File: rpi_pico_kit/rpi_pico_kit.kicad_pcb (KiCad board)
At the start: 2 copper layers, 99.1 x 99.1 mm, 200 parts, among them J1 DC Jack 5.5x2.1mm, J10 OLED Display SSD1306, J11 Conn_01x04_Male, J12 Conn_01x04_Male, J13 AudioJack-CUI-SJ-3523-SMT, J14 AudioJack-CUI-SJ-3523-SMT, J2 USB_B, J3 Conn_01x03_Male, J4 DB15_Female, J5 HDMI_A, J6 Conn_01x08_Male, J7 Conn_01x08_Male, J8 Conn_01x08_Male, J9 Micro_SD_Card_Det, Q1 DMN63D8L-7, Q2 DMN63D8L-7, Q3 DMN63D8L-7, Q4 DMN63D8L-7, Q5 DMN63D8L-7, Q6 DMN63D8L-7, Q7 DMN63D8L-7, SW1 SW_Push, SW10 SW_Push, SW2 RotaryEncoder_Switch, SW3 SW_Push, SW4 SW_Push, SW5 SW_Push, SW6 SW_Push, SW7 SW_Push, SW8 SW_Push, SW9 SW_Push, U1 RPi Pico, U10 74LVC2G34GV, U11 PCM5101A, U2 NCP1117-3.3_SOT223, U3 RP2040, U4 W25Q16JVSSIQ, U5 74HC14, U6 74HC14, U7 MCP23S08-xSO, U8 AT24CS32, U9 NCP115-3.3_SOT23-5, Y1 12MHz

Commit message: pcb changes
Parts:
- removed JP2, JP3, JP4, JP5, JP6: SolderJumper_2_Bridged, Jumper:SolderJumper-2_P1.3mm_Bridged_RoundedPad1.0x1.5mm
- TP3: footprint TestPoint:TestPoint_Pad_D1.5mm -> TestPoint:TestPoint_Pad_D1.0mm
- moved LED2 140.2 mm to (149.4, -14.7)
- moved LED3 128.2 mm to (149.2, -10.7)
- moved LED4 128.2 mm to (149.2, -6.86)
- moved R1 121.4 mm to (24.3, 34.0)
- moved D3 80.4 mm to (126.0, -19.6)
- moved R17 77.0 mm to (126.0, -12.7)
- moved R18 67.1 mm to (126.0, -9.65)
- moved R6 60.3 mm to (82.0, 50.8)
- moved RN3 59.2 mm to (97.3, 57.4)
- moved C18 57.4 mm to (126.0, -6.60)
- moved JP1 54.1 mm to (27.9, -6.86)
- moved R14 51.8 mm to (27.9, -10.4)
- moved R16 50.8 mm to (126.0, -15.7)
- moved C3 47.5 mm to (76.7, -13.0)
- moved Y1 47.1 mm to (90.2, 24.4)
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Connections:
- R13 pad 2: Net-(JP6-A) -> /~{RESET}
- RN14 pad 5: Net-(JP3-A) -> /SWDIO
- RN14 pad 6: Net-(JP2-A) -> /SWCLK
- U3 pad 6: Net-(JP4-A) -> /DEBUGGER_RX
- U3 pad 7: Net-(JP5-A) -> /DEBUGGER_TX

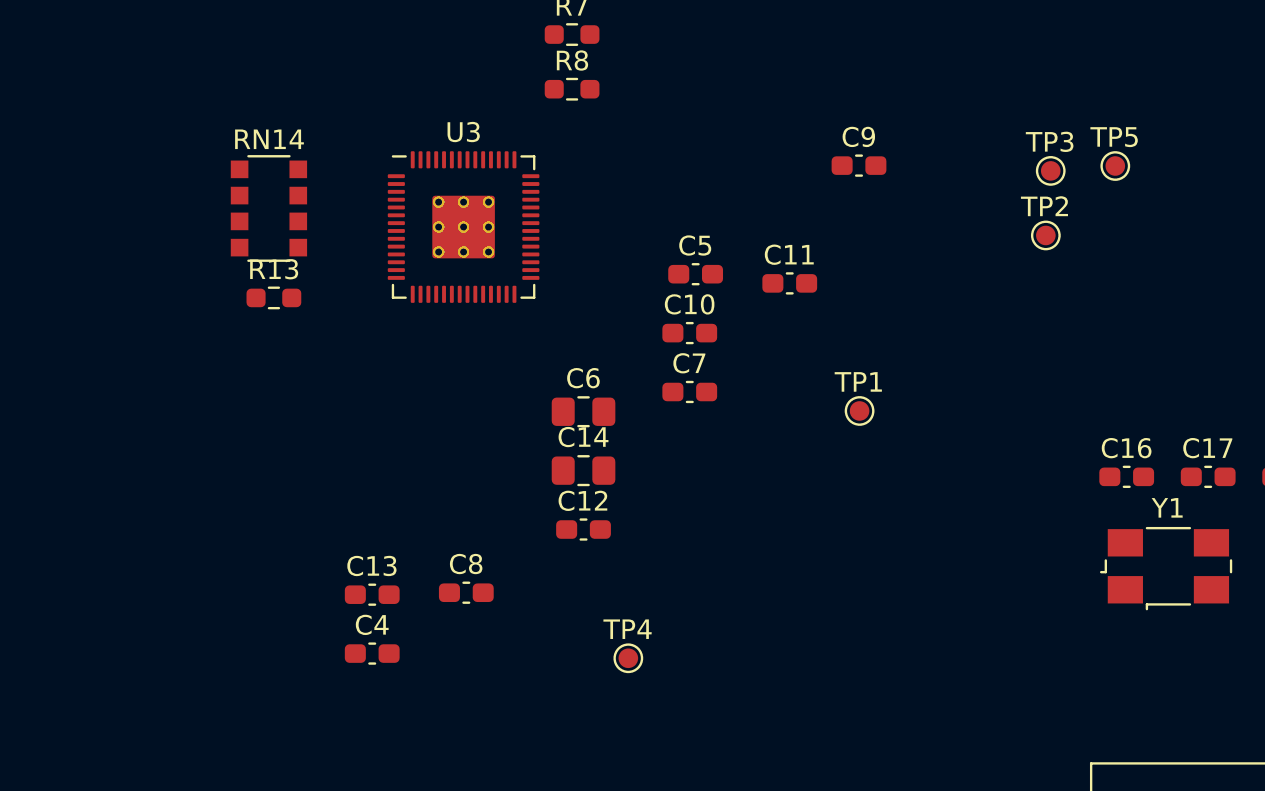
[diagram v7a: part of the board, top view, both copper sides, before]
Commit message: rearranged parts to blocks
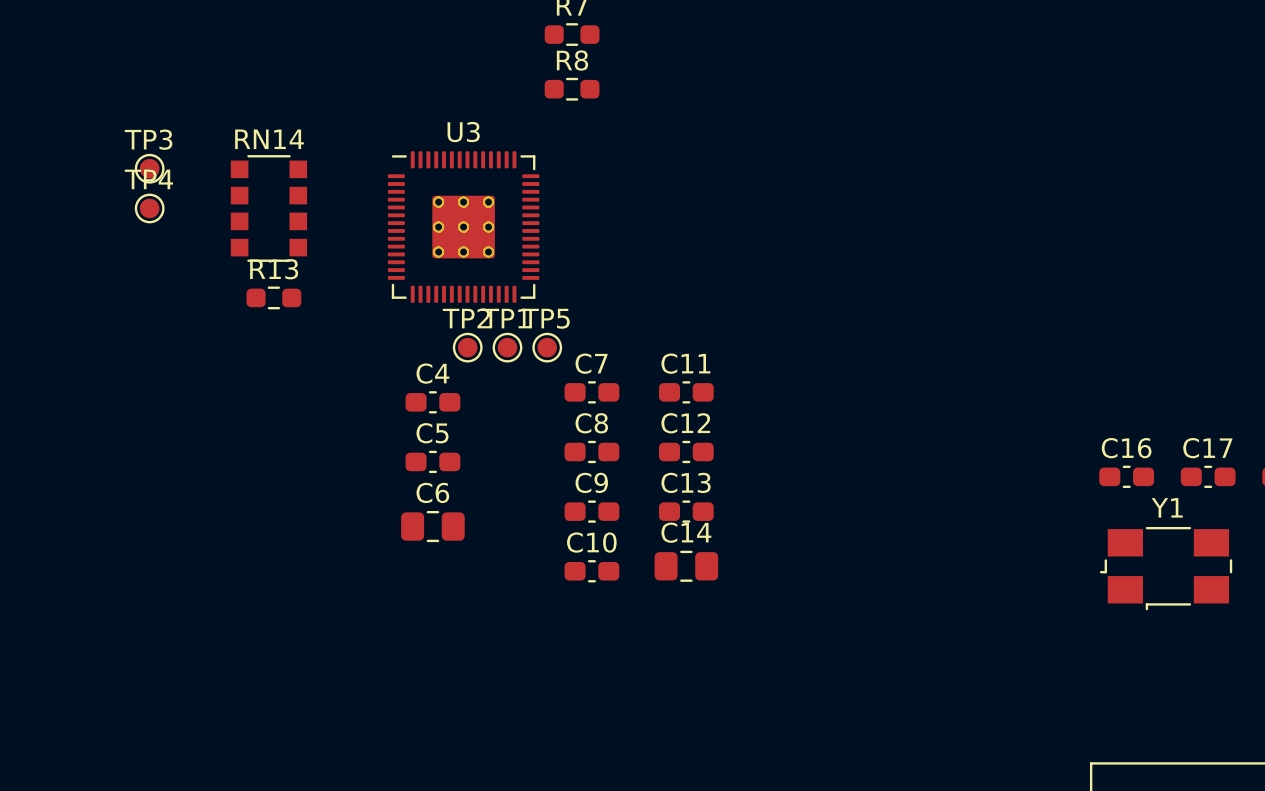
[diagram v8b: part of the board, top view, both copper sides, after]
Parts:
- moved TP3 46.1 mm to (38.1, 4.06)
- moved TP4 33.6 mm to (38.1, 6.10)
- moved TP5 30.5 mm to (58.4, 13.2)
- moved TP2 30.1 mm to (54.4, 13.2)
- moved C9 22.3 mm to (60.7, 21.6)
- moved TP1 18.3 mm to (56.4, 13.2)
- moved C13 16.6 mm to (65.5, 21.6)
- moved C5 16.5 mm to (52.6, 19.1)
- moved C4 13.2 mm to (52.6, 16.0)
- moved C10 13.2 mm to (60.7, 24.6)
- moved C6 9.68 mm to (52.6, 22.4)
- moved C8 9.64 mm to (60.7, 18.5)
- moved C11 7.68 mm to (65.5, 15.5)
- moved C14 7.18 mm to (65.5, 24.4)
- moved C12 6.58 mm to (65.5, 18.5)
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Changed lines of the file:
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@@
   )
   (footprint "TestPoint:TestPoint_Pad_D1.0mm" (layer "F.Cu")
-    (at 83.905 7.475)
+    (at 54.356 13.208)
     (descr "SMD pad as test Point, diameter 1.0mm")
     (tags "test point SMD pad")
@@
   )
   (footprint "Capacitor_SMD:C_0805_2012Metric_Pad1.18x1.45mm_HandSolder" (layer "F.Cu")
-    (at 60.275 19.495)
+    (at 65.532 24.384)
     (descr "Capacitor SMD 0805 (2012 Metric), square (rectangular) end terminal, IPC_7351 nominal with elongated pad for handsoldering. (Body size source: IPC-SM-782 page 76, https://www.pcb-3d.com/wordpress/wp-content/uploads/ipc-sm-782a_amendment_1_and_2.pdf, https://docs.google.com/spreadsheets/d/1BsfQQcO9C6DZCsRaXUlFlo91Tg2WpOkGARC1WS5S8t0/edit?usp=sharing), generated with kicad-footprint-generator")
     (tags "capacitor handsolder")
@@
   )
   (footprint "TestPoint:TestPoint_Pad_D1.0mm" (layer "F.Cu")
-    (at 84.155 4.175)
+    (at 38.1 4.064)
     (descr "SMD pad as test Point, diameter 1.0mm")
     (tags "test point SMD pad")
@@
   )
   (footprint "Capacitor_SMD:C_0603_1608Metric_Pad1.08x0.95mm_HandSolder" (layer "F.Cu")
-    (at 54.285 25.735)
+    (at 60.706 18.542)
     (descr "Capacitor SMD 0603 (1608 Metric), square (rectangular) end terminal, IPC_7351 nominal with elongated pad for handsoldering. (Body size source: IPC-SM-782 page 76, https://www.pcb-3d.com/wordpress/wp-content/uploads/ipc-sm-782a_amendment_1_and_2.pdf), generated with kicad-footprint-generator")
     (tags "capacitor handsolder")
@@
   )
   (footprint "Capacitor_SMD:C_0603_1608Metric_Pad1.08x0.95mm_HandSolder" (layer "F.Cu")
-    (at 74.355 3.905)
+    (at 60.706 21.59)
     (descr "Capacitor SMD 0603 (1608 Metric), square (rectangular) end terminal, IPC_7351 nominal with elongated pad for handsoldering. (Body size source: IPC-SM-782 page 76, https://www.pcb-3d.com/wordpress/wp-content/uploads/ipc-sm-782a_amendment_1_and_2.pdf), generated with kicad-footprint-generator")
     (tags "capacitor handsolder")
@@
   )
   (footprint "Capacitor_SMD:C_0603_1608Metric_Pad1.08x0.95mm_HandSolder" (layer "F.Cu")
-    (at 65.705 12.465)
+    (at 60.706 24.638)
     (descr "Capacitor SMD 0603 (1608 Metric), square (rectangular) end terminal, IPC_7351 nominal with elongated pad for handsoldering. (Body size source: IPC-SM-782 page 76, https://www.pcb-3d.com/wordpress/wp-content/uploads/ipc-sm-782a_amendment_1_and_2.pdf), generated with kicad-footprint-generator")
     (tags "capacitor handsolder")
@@
   )
   (footprint "Capacitor_SMD:C_0603_1608Metric_Pad1.08x0.95mm_HandSolder" (layer "F.Cu")
-    (at 66.005 9.455)
+    (at 52.578 19.05)
     (descr "Capacitor SMD 0603 (1608 Metric), square (rectangular) end terminal, IPC_7351 nominal with elongated pad for handsoldering. (Body size source: IPC-SM-782 page 76, https://www.pcb-3d.com/wordpress/wp-content/uploads/ipc-sm-782a_amendment_1_and_2.pdf), generated with kicad-footprint-generator")
     (tags "capacitor handsolder")
@@
   )
   (footprint "Capacitor_SMD:C_0603_1608Metric_Pad1.08x0.95mm_HandSolder" (layer "F.Cu")
-    (at 65.705 15.475)
+    (at 60.706 15.494)
     (descr "Capacitor SMD 0603 (1608 Metric), square (rectangular) end terminal, IPC_7351 nominal with elongated pad for handsoldering. (Body size source: IPC-SM-782 page 76, https://www.pcb-3d.com/wordpress/wp-content/uploads/ipc-sm-782a_amendment_1_and_2.pdf), generated with kicad-footprint-generator")
     (tags "capacitor handsolder")
@@
   )
   (footprint "TestPoint:TestPoint_Pad_D1.0mm" (layer "F.Cu")
-    (at 62.565 29.085)
+    (at 38.1 6.096)
     (descr "SMD pad as test Point, diameter 1.0mm")
     (tags "test point SMD pad")
@@
   )
   (footprint "Capacitor_SMD:C_0603_1608Metric_Pad1.08x0.95mm_HandSolder" (layer "F.Cu")
-    (at 49.475 25.835)
+    (at 65.532 21.59)
     (descr "Capacitor SMD 0603 (1608 Metric), square (rectangular) end terminal, IPC_7351 nominal with elongated pad for handsoldering. (Body size source: IPC-SM-782 page 76, https://www.pcb-3d.com/wordpress/wp-content/uploads/ipc-sm-782a_amendment_1_and_2.pdf), generated with kicad-footprint-generator")
     (tags "capacitor handsolder")
@@
   )
   (footprint "TestPoint:TestPoint_Pad_D1.0mm" (layer "F.Cu")
-    (at 87.455 3.925)
+    (at 58.42 13.208)
     (descr "SMD pad as test Point, diameter 1.0mm")
     (tags "test point SMD pad")
@@
   )
   (footprint "TestPoint:TestPoint_Pad_D1.0mm" (layer "F.Cu")
-    (at 74.385 16.445)
+    (at 56.388 13.208)
     (descr "SMD pad as test Point, diameter 1.0mm")
     (tags "test point SMD pad")
@@
   )
   (footprint "Capacitor_SMD:C_0603_1608Metric_Pad1.08x0.95mm_HandSolder" (layer "F.Cu")
-    (at 49.475 28.845)
+    (at 52.578 16.002)
     (descr "Capacitor SMD 0603 (1608 Metric), square (rectangular) end terminal, IPC_7351 nominal with elongated pad for handsoldering. (Body size source: IPC-SM-782 page 76, https://www.pcb-3d.com/wordpress/wp-content/uploads/ipc-sm-782a_amendment_1_and_2.pdf), generated with kicad-footprint-generator")
     (tags "capacitor handsolder")
@@
   )
   (footprint "Capacitor_SMD:C_0805_2012Metric_Pad1.18x1.45mm_HandSolder" (layer "F.Cu")
-    (at 60.275 16.485)
+    (at 52.578 22.352)
     (descr "Capacitor SMD 0805 (2012 Metric), square (rectangular) end terminal, IPC_7351 nominal with elongated pad for handsoldering. (Body size source: IPC-SM-782 page 76, https://www.pcb-3d.com/wordpress/wp-content/uploads/ipc-sm-782a_amendment_1_and_2.pdf, https://docs.google.com/spreadsheets/d/1BsfQQcO9C6DZCsRaXUlFlo91Tg2WpOkGARC1WS5S8t0/edit?usp=sharing), generated with kicad-footprint-generator")
     (tags "capacitor handsolder")
@@
   )
   (footprint "Capacitor_SMD:C_0603_1608Metric_Pad1.08x0.95mm_HandSolder" (layer "F.Cu")
-    (at 70.815 9.925)
+    (at 65.532 15.494)
     (descr "Capacitor SMD 0603 (1608 Metric), square (rectangular) end terminal, IPC_7351 nominal with elongated pad for handsoldering. (Body size source: IPC-SM-782 page 76, https://www.pcb-3d.com/wordpress/wp-content/uploads/ipc-sm-782a_amendment_1_and_2.pdf), generated with kicad-footprint-generator")
     (tags "capacitor handsolder")
@@
   )
   (footprint "Capacitor_SMD:C_0603_1608Metric_Pad1.08x0.95mm_HandSolder" (layer "F.Cu")
-    (at 60.275 22.505)
+    (at 65.532 18.542)
     (descr "Capacitor SMD 0603 (1608 Metric), square (rectangular) end terminal, IPC_7351 nominal with elongated pad for handsoldering. (Body size source: IPC-SM-782 page 76, https://www.pcb-3d.com/wordpress/wp-content/uploads/ipc-sm-782a_amendment_1_and_2.pdf), generated with kicad-footprint-generator")
     (tags "capacitor handsolder")
